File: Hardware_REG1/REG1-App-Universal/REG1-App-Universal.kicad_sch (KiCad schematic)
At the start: 2 parts, among them J1 REG1_App_Connector, J2 Conn_01x10

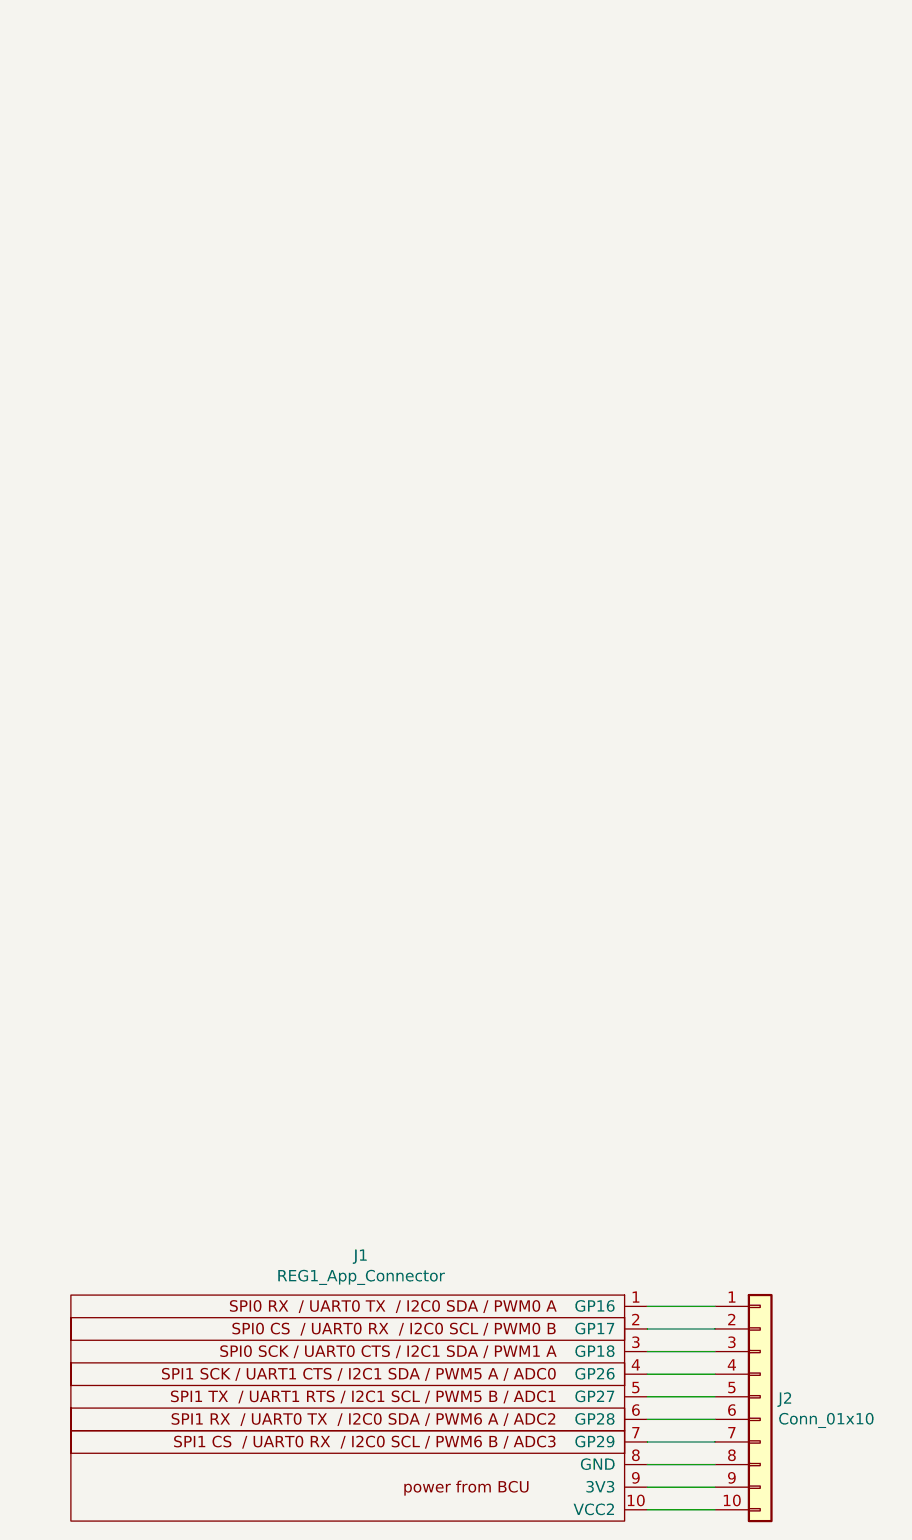
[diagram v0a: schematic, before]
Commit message: added DALI lib
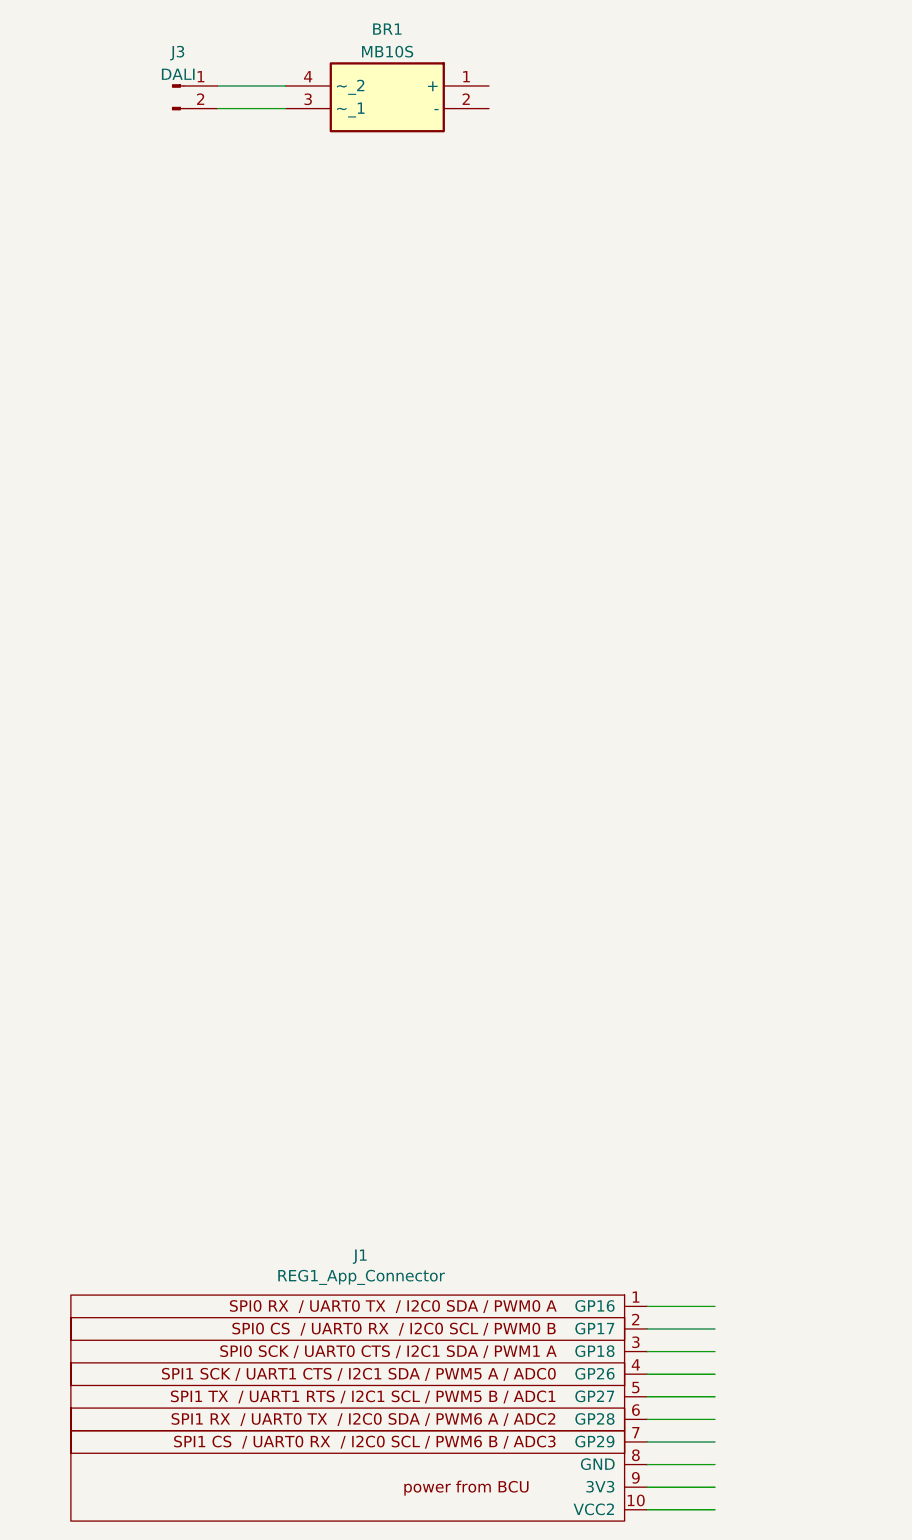
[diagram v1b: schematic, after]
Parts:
- removed J2: Conn_01x10, Connector_PinHeader_2.54mm:PinHeader_1x10_P2.54mm_Vertical, symbol Connector_Generic:Conn_01x10
- added BR1: MB10S, SOP245P670X290-4N, symbol DALI:MB10S
- added J3: DALI, TerminalBlock_4Ucon:TerminalBlock_4Ucon_1x02_P3.50mm_Horizontal, symbol Connector:Conn_01x02_Pin
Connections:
- new net: BR1.3 (~_1), J3.2 (Pin_2)
- new net: BR1.4 (~_2), J3.1 (Pin_1)
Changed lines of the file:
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@@
     (comment 4 "https://OpenKNX.de")
+  )
+  (wire (pts (xy 35.56 33.02) (xy 43.18 33.02))
+    (stroke (width 0) (type default))
   )
   (wire (pts (xy 91.44 175.26) (xy 83.82 175.26))
@@
   )
   (wire (pts (xy 91.44 187.96) (xy 83.82 187.96))
+    (stroke (width 0) (type default))
+  )
+  (wire (pts (xy 35.56 30.48) (xy 43.18 30.48))
     (stroke (width 0) (type default))
   )
@@
   (wire (pts (xy 83.82 172.72) (xy 91.44 172.72))
     (stroke (width 0) (type default))
-  )
-  (symbol (lib_id "Connector_Generic:Conn_01x10") (at 96.52 177.8 0) (unit 1)
-    (in_bom yes) (on_board yes) (dnp no)
-    (property "Reference" "J2" (at 98.552 178.0032 0)
-      (effects (font (size 1.27 1.27)) (justify left))
-    )
-    (property "Value" "Conn_01x10" (at 98.552 180.3146 0)
-      (effects (font (size 1.27 1.27)) (justify left))
-    )
-    (property "Footprint" "Connector_PinHeader_2.54mm:PinHeader_1x10_P2.54mm_Vertical" (at 96.52 177.8 0)
-      (effects (font (size 1.27 1.27)) hide)
-    )
-    (property "Datasheet" "~" (at 96.52 177.8 0)
-      (effects (font (size 1.27 1.27)) hide)
-    )
-    (pin "1")
-    (pin "10")
-    (pin "2")
-    (pin "3")
-    (pin "4")
-    (pin "5")
-    (pin "6")
-    (pin "7")
-    (pin "8")
-    (pin "9")
-    (instances
-      (project "REG1-App-Universal"
-        (path "/a0393b09-4b2d-4a64-98b7-96bb7f245f9d"
-          (reference "J2") (unit 1)
-        )
-      )
-    )
   )
   (symbol (lib_id "OpenKNX:REG1_App_Connector") (at 68.58 179.07 0) (unit 1)
@@
         )
       )
+    )
+  )
+  (symbol (lib_id "DALI:MB10S") (at 66.04 30.48 0) (mirror y) (unit 1)
+    (in_bom yes) (on_board yes) (dnp no)
+    (property "Reference" "BR1" (at 54.61 24.13 0)
+      (effects (font (size 1.27 1.27)))
+    )
+    (property "Value" "MB10S" (at 54.61 26.67 0)
+      (effects (font (size 1.27 1.27)))
+    )
+    (property "Footprint" "SOP245P670X290-4N" (at 46.99 125.4 0)
+      (effects (font (size 1.27 1.27)) (justify left top) hide)
+    )
+    (property "Datasheet" "http://www.onsemi.com/pub/Collateral/MB10S-D.pdf" (at 46.99 225.4 0)
+      (effects (font (size 1.27 1.27)) (justify left top) hide)
+    )
+    (property "Height" "2.9" (at 46.99 425.4 0)
+      (effects (font (size 1.27 1.27)) (justify left top) hide)
+    )
+    (property "Manufacturer_Name" "onsemi" (at 46.99 525.4 0)
+      (effects (font (size 1.27 1.27)) (justify left top) hide)
+    )
+    (property "Manufacturer_Part_Number" "MB10S" (at 46.99 625.4 0)
+      (effects (font (size 1.27 1.27)) (justify left top) hide)
+    )
+    (property "Mouser Part Number" "512-MB10S" (at 46.99 725.4 0)
+      (effects (font (size 1.27 1.27)) (justify left top) hide)
+    )
+    (property "Mouser Price/Stock" "https://www.mouser.co.uk/ProductDetail/onsemi-Fairchild/MB10S?qs=FHGIxCZCr7o%252BnYB0V%2FNH8A%3D%3D" (at 46.99 825.4 0)
+      (effects (font (size 1.27 1.27)) (justify left top) hide)
+    )
+    (property "Arrow Part Number" "MB10S" (at 46.99 925.4 0)
+      (effects (font (size 1.27 1.27)) (justify left top) hide)
+    )
+    (property "Arrow Price/Stock" "https://www.arrow.com/en/products/mb10s/on-semiconductor?region=nac" (at 46.99 1025.4 0)
+      (effects (font (size 1.27 1.27)) (justify left top) hide)
+    )
+    (pin "1")
+    (pin "2")
+    (pin "3")
+    (pin "4")
+    (instances
+      (project "REG1-App-Universal"
+        (path "/a0393b09-4b2d-4a64-98b7-96bb7f245f9d"
+          (reference "BR1") (unit 1)
+        )
+      )
+    )
+  )
+  (symbol (lib_id "Connector:Conn_01x02_Pin") (at 30.48 30.48 0) (unit 1)
+    (in_bom yes) (on_board yes) (dnp no) (fields_autoplaced)
+    (property "Reference" "J3" (at 31.115 26.67 0)
+      (effects (font (size 1.27 1.27)))
+    )
+    (property "Value" "DALI" (at 31.115 29.21 0)
+      (effects (font (size 1.27 1.27)))
+    )
+    (property "Footprint" "TerminalBlock_4Ucon:TerminalBlock_4Ucon_1x02_P3.50mm_Horizontal" (at 30.48 30.48 0)
+      (effects (font (size 1.27 1.27)) hide)
+    )
+    (property "Datasheet" "~" (at 30.48 30.48 0)
+      (effects (font (size 1.27 1.27)) hide)
+    )
+    (pin "1")
+    (pin "2")
+    (instances
+      (project "REG1-App-Universal"
+        (path "/a0393b09-4b2d-4a64-98b7-96bb7f245f9d"
+          (reference "J3") (unit 1)
+        )
+      )

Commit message: updated pcb
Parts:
- added C1: 1n, Capacitor_SMD:C_0603_1608Metric, symbol Device:C
- added C2: 2.2u, Capacitor_SMD:C_0805_2012Metric, symbol Device:C
- added D1: 1SMA4746, DIOM4325X250N, symbol DALI:1SMA4746
- added D2: D_Zener_Small, Diode_SMD:D_SOD-123, symbol Device:D_Zener_Small
- added D3: UDZSTE-175.6B, SODFL2512X90N, symbol DALI:UDZSTE-175.6B
- added D4: LED, LED_SMD:LED_0603_1608Metric, symbol Device:LED
- added Q1: BSS123, DALI:SOT23, symbol DALI:BSS123
- added Q2: BC857, Package_TO_SOT_SMD:SOT-23, symbol Transistor_BJT:BC857
- added R1, R2, R4, R5: 100k, Resistor_SMD:R_1206_3216Metric, symbol Device:R
- added R10: 1k, Resistor_SMD:R_1206_3216Metric, symbol Device:R
- added R11: 300, Resistor_SMD:R_1206_3216Metric, symbol Device:R
- added R3: 390, Resistor_SMD:R_0603_1608Metric, symbol Device:R
- added R6: 16k, Resistor_SMD:R_0805_2012Metric, symbol Device:R
- added R7, R8, R9: 4.7k, Resistor_SMD:R_0603_1608Metric, symbol Device:R
- added U1, U2: EL357N(A)(TA)-G, SOP254P700X200-4N, symbol DALI:EL357N(A)(TA)-G
- added U3: STN93003, SOT230P700X180-4N, symbol DALI:STN93003
- added U4: STN1HNK60, SOT-223, symbol DALI:STN1HNK60
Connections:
- net D_RX: now reaches J1.1 (GP16)
- net D_RX: now also R8.2, R9.2, U1.4
- net D_TX: now reaches J1.2 (GP17)
- net D_TX: now also R11.2
- net GND: now reaches J1.8 (GND)
- net GND: now also U1.3, U2.2
- net +3.3V: now reaches J1.9 (3V3)
- net +3.3V: now also D4.2 (A), R9.1
- net Dali+: now reaches BR1.1 (+)
- net Dali+: now also Q2.2 (E), R3.1, R4.2, U4.2, U4.4
- net DALI-: now reaches BR1.2 (-)
- net DALI-: now also C1.2, C2.2, D1.A, D3.A, Q1.2, R1.1, R6.1, R7.1, U4.3
- new net: Q2.1 (B), R3.2, U3.3
- new net: C2.1, D3.C, U1.2, U2.4
- new net: D1.C, D2.2 (A), Q1.1, R6.2
- new net: D2.1 (K), R5.1
- new net: R4.1, R5.2
- new net: Q2.3 (C), R2.2, U3.1
- new net: R10.1, U2.1
- new net: R10.2, R11.1
- new net: D4.1 (K), R8.1
- new net: C1.1, Q1.3, R7.2, U2.3, U4.1
- new net: U1.1, U3.2, U3.4
- new net: R1.2, R2.1
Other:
- moved on the sheet: BR1, J3
